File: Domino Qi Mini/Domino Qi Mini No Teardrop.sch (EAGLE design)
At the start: 90 parts, among them J1 MH22-1, J2 MH22-1, M1 DOMINO, Q1 AP2302GN, Q2 2SC4081, SW1 IT-1210, SW2 IT-1210, SW3 IT-1210, U1 MP65151DJ, U2 ATMEGA32U4-XUAU/MU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

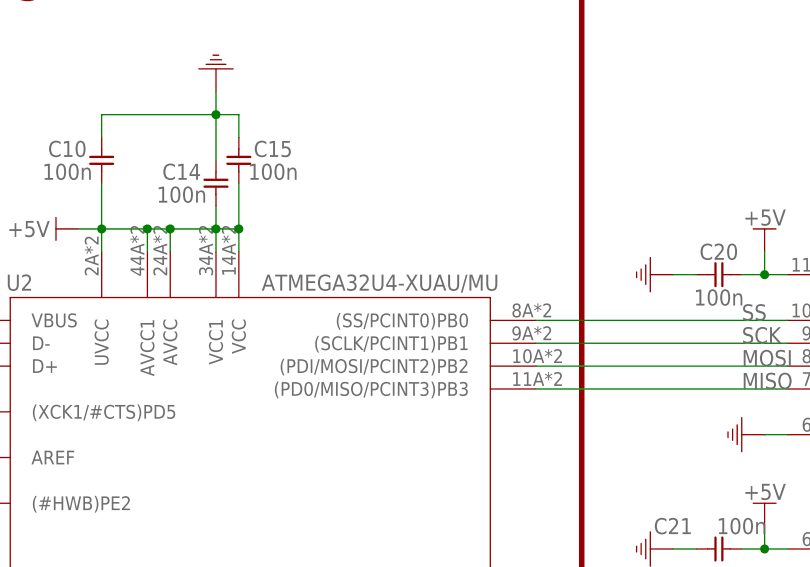
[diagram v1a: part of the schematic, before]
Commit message: Domino Qi Mini Rev. A: added BOM and a few datasheets
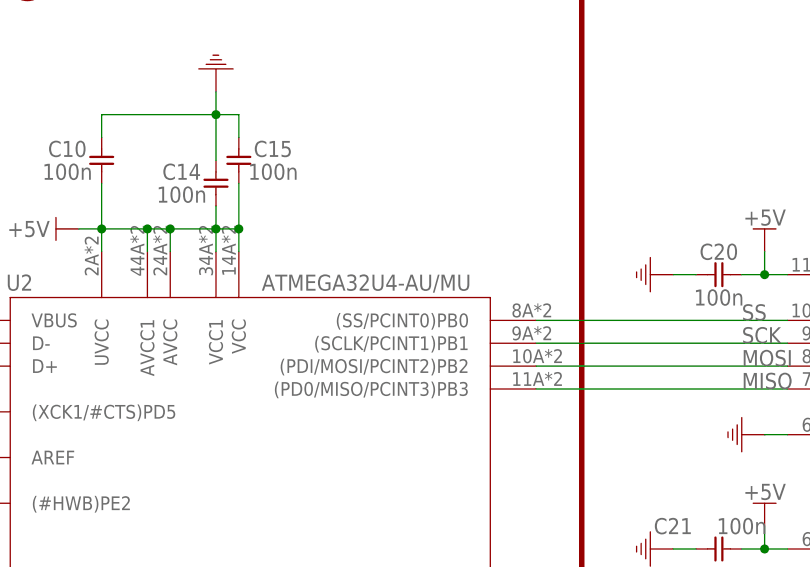
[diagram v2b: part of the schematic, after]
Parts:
- A1: BOM (none) -> EXCLUDE; PARTNO (none) -> RF_ANT1
- C8: PARTNO C0402_2u2_X5R_20%_CER_6V3 -> C0402_2u2_X5R_10%_CER_6V3; TOL ±20% -> ±10%
- J1, J2: PARTNO (none) -> MH22-1-0.1
- Q1: PARTNO (none) -> AP2302GN
- Q2: PARTNO (none) -> 2SC4081
- SW1, SW2, SW3: PARTNO (none) -> IT-1210
- U2: value ATMEGA32U4-XUAU/MU -> ATMEGA32U4-AU/MU; device Domino:ATMEGA32U4-XUAU/MU -> Domino:ATMEGA32U4-AU/MU; PARTNO (none) -> ATMEGA32U4-MU
- U4: PARTNO (none) -> NTB0104GU12
- U5: PARTNO (none) -> NTB0102GU
- U6: PARTNO (none) -> MAX3375EEKA+T
- Y1: PARTNO (none) -> CRYSTAL_16MHZ_32X25_2SH_12PF_30PPM
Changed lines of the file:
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@@
 <?xml version="1.0" encoding="utf-8"?>
 <!DOCTYPE eagle SYSTEM "eagle.dtd">
-<eagle version="7.0.0">
+<eagle version="6.5.0">
 <drawing>
 <settings>
@@
 </part>
 <part name="SUPPLY17" library="Domino" deviceset="GND" device=""/>
-<part name="U2" library="Domino" deviceset="ATMEGA32U4-XU" device="AU/MU" value="ATMEGA32U4-XUAU/MU"/>
+<part name="U2" library="Domino" deviceset="ATMEGA32U4-" device="AU/MU" value="ATMEGA32U4-AU/MU">
+<attribute name="PARTNO" value="ATMEGA32U4-MU"/>
+</part>
 <part name="U$8" library="Domino" deviceset="+5V" device=""/>
 <part name="C15" library="Domino" deviceset="CAP_" device="0402" value="100n">
@@
 <attribute name="VOLT" value="50V"/>
 </part>
-<part name="Y1" library="Domino" deviceset="CRYSTAL_2SH" device="" value="16MHz"/>
+<part name="Y1" library="Domino" deviceset="CRYSTAL_2SH" device="" value="16MHz">
+<attribute name="PARTNO" value="CRYSTAL_16MHZ_32X25_2SH_12PF_30PPM"/>
+</part>
 <part name="R2" library="Domino" deviceset="RES_" device="0402" value="22R">
 <attribute name="PARTNO" value="R0402_22R_5%_62.5mW"/>
@@
 <attribute name="VOLT" value="50V"/>
 </part>
-<part name="U4" library="Domino" deviceset="NTB0104" device="GU12"/>
-<part name="U5" library="Domino" deviceset="NTB0102" device="GU"/>
-<part name="U6" library="Domino" deviceset="MAX3375E" device="EKA+T"/>
+<part name="U4" library="Domino" deviceset="NTB0104" device="GU12">
+<attribute name="PARTNO" value="NTB0104GU12"/>
+</part>
+<part name="U5" library="Domino" deviceset="NTB0102" device="GU">
+<attribute name="PARTNO" value="NTB0102GU"/>
+</part>
+<part name="U6" library="Domino" deviceset="MAX3375E" device="EKA+T">
+<attribute name="PARTNO" value="MAX3375EEKA+T"/>
+</part>
 <part name="U$6" library="Domino" deviceset="+5V" device=""/>
 <part name="U$10" library="Domino" deviceset="+5V" device=""/>
@@
 </part>
 <part name="SUPPLY47" library="Domino" deviceset="GND" device=""/>
-<part name="Q2" library="Domino" deviceset="2SC4081" device=""/>
+<part name="Q2" library="Domino" deviceset="2SC4081" device="">
+<attribute name="PARTNO" value="2SC4081"/>
+</part>
 <part name="R12" library="Domino" deviceset="RES_" device="0402" value="10k">
 <attribute name="PARTNO" value="R0402_10k_5%_62.5mW"/>
@@
 <attribute name="VOLT" value="25V"/>
 </part>
-<part name="Q1" library="Domino" deviceset="AP2302GN" device=""/>
+<part name="Q1" library="Domino" deviceset="AP2302GN" device="">
+<attribute name="PARTNO" value="AP2302GN"/>
+</part>
 <part name="U$16" library="Domino" deviceset="+5V" device=""/>
 <part name="C8" library="Domino" deviceset="CAP_" device="0805" value="2u2">
-<attribute name="PARTNO" value="C0402_2u2_X5R_20%_CER_6V3"/>
+<attribute name="PARTNO" value="C0402_2u2_X5R_10%_CER_6V3"/>
 <attribute name="SIZE" value="0402"/>
 <attribute name="TC" value="X5R"/>
-<attribute name="TOL" value="±20%"/>
+<attribute name="TOL" value="±10%"/>
 <attribute name="TYPE" value="CER"/>
 <attribute name="VOLT" value="6.3V"/>
@@
 <part name="U$2" library="Domino" deviceset="+5V" device=""/>
 <part name="SUPPLY13" library="Domino" deviceset="GND" device=""/>
-<part name="J2" library="Domino" deviceset="MH22-1" device=""/>
-<part name="SW3" library="Domino" deviceset="IT-1210" device=""/>
-<part name="SW2" library="Domino" deviceset="IT-1210" device=""/>
-<part name="SW1" library="Domino" deviceset="IT-1210" device=""/>
+<part name="J2" library="Domino" deviceset="MH22-1" device="">
+<attribute name="PARTNO" value="MH22-1-0.1"/>
+</part>
+<part name="SW3" library="Domino" deviceset="IT-1210" device="">
+<attribute name="PARTNO" value="IT-1210"/>
+</part>
+<part name="SW2" library="Domino" deviceset="IT-1210" device="">
+<attribute name="PARTNO" value="IT-1210"/>
+</part>
+<part name="SW1" library="Domino" deviceset="IT-1210" device="">
+<attribute name="PARTNO" value="IT-1210"/>
+</part>
 <part name="W1" library="Domino" deviceset="DOMINO_QI_LOGO" device=""/>
-<part name="A1" library="Domino" deviceset="RF_ANT1" device=""/>
-<part name="J1" library="Domino" deviceset="MH22-1" device=""/>
+<part name="A1" library="Domino" deviceset="RF_ANT1" device="">
+<attribute name="BOM" value="EXCLUDE"/>
+<attribute name="PARTNO" value="RF_ANT1"/>
+</part>
+<part name="J1" library="Domino" deviceset="MH22-1" device="">
+<attribute name="PARTNO" value="MH22-1-0.1"/>
+</part>
 <part name="C2" library="Domino" deviceset="CAP_" device="0402" value="100n">
 <attribute name="PARTNO" value="C0402_100n_X7R_10%_CER_50V"/>
@@
 <attribute name="VALUE" x="91.44" y="160.02" size="1.778" layer="96" rot="MR180"/>
 <attribute name="NAME" x="66.04" y="158.242" size="1.778" layer="95" rot="MR0"/>
+<attribute name="PARTNO" x="91.44" y="88.9" size="1.778" layer="96" rot="MR0" display="off"/>
 </instance>
 <instance part="U$8" gate="G$1" x="71.12" y="165.1" smashed="yes" rot="R90">
@@
 <attribute name="NAME" x="41.656" y="101.6" size="1.778" layer="95"/>
 <attribute name="VALUE" x="41.656" y="99.06" size="1.778" layer="96"/>
+<attribute name="PARTNO" x="50.8" y="106.68" size="1.778" layer="96" rot="R270" display="off"/>
 </instance>
 <instance part="R2" gate="G$1" x="50.8" y="152.4" smashed="yes">
@@
 <attribute name="NAME" x="154.94" y="165.1" size="1.778" layer="95" rot="MR180" align="center-left"/>
 <attribute name="VALUE" x="162.56" y="165.1" size="1.778" layer="96" rot="MR180" align="center-left"/>
+<attribute name="PARTNO" x="165.1" y="149.86" size="1.778" layer="96" rot="MR0" display="off"/>
 </instance>
 <instance part="U5" gate="G$1" x="165.1" y="121.92" smashed="yes" rot="MR0">
 <attribute name="NAME" x="154.94" y="134.62" size="1.778" layer="95" rot="MR180" align="center-left"/>
 <attribute name="VALUE" x="162.56" y="134.62" size="1.778" layer="96" rot="MR180" align="center-left"/>
+<attribute name="PARTNO" x="165.1" y="121.92" size="1.778" layer="96" rot="MR0" display="off"/>
 </instance>
 <instance part="U6" gate="G$1" x="167.64" y="101.6" smashed="yes">
 <attribute name="NAME" x="154.94" y="111.76" size="1.778" layer="95" align="center-left"/>
 <attribute name="VALUE" x="162.56" y="111.76" size="1.778" layer="96" align="center-left"/>
+<attribute name="PARTNO" x="167.64" y="101.6" size="1.778" layer="96" display="off"/>
 </instance>
 <instance part="U$6" gate="G$1" x="147.32" y="162.56" smashed="yes">
@@
 <attribute name="NAME" x="170.18" y="83.82" size="1.778" layer="95" rot="MR0"/>
 <attribute name="VALUE" x="170.18" y="81.28" size="1.778" layer="96" rot="MR0"/>
+<attribute name="PARTNO" x="172.72" y="83.82" size="1.778" layer="96" rot="MR0" display="off"/>
 </instance>
 <instance part="R12" gate="G$1" x="162.56" y="93.98" smashed="yes" rot="R180">
@@
 <attribute name="VALUE" x="163.83" y="39.37" size="1.778" layer="96" rot="MR0" align="center"/>
 <attribute name="NAME" x="163.83" y="41.91" size="1.778" layer="95" rot="MR0" align="center"/>
+<attribute name="PARTNO" x="157.48" y="35.56" size="1.778" layer="96" rot="MR0" display="off"/>
 </instance>
 <instance part="U$16" gate="G$1" x="55.88" y="175.26" smashed="yes">
@@
 <attribute name="VALUE" x="318.135" y="40.64" size="1.778" layer="96" rot="R180" align="center"/>
 <attribute name="NAME" x="314.96" y="43.053" size="1.778" layer="95" rot="R180" align="center"/>
+<attribute name="PARTNO" x="281.94" y="43.18" size="1.778" layer="96" rot="R90" display="off"/>
 </instance>
 <instance part="SW3" gate="G$1" x="299.72" y="185.42" smashed="yes" rot="MR0">
 <attribute name="NAME" x="302.26" y="193.04" size="1.778" layer="95" rot="MR180"/>
 <attribute name="VALUE" x="302.26" y="190.5" size="1.778" layer="96" rot="MR180"/>
+<attribute name="PARTNO" x="299.72" y="185.42" size="1.778" layer="96" rot="MR0" display="off"/>
 </instance>
 <instance part="SW2" gate="G$1" x="231.14" y="91.44" smashed="yes">
 <attribute name="NAME" x="228.6" y="99.06" size="1.778" layer="95" rot="R180"/>
 <attribute name="VALUE" x="228.6" y="96.52" size="1.778" layer="96" rot="R180"/>
+<attribute name="PARTNO" x="231.14" y="91.44" size="1.778" layer="96" display="off"/>
 </instance>
 <instance part="SW1" gate="G$1" x="109.22" y="25.4" smashed="yes" rot="MR0">
 <attribute name="NAME" x="106.68" y="30.48" size="1.778" layer="95" rot="MR0"/>
 <attribute name="VALUE" x="106.68" y="27.94" size="1.778" layer="96" rot="MR0"/>
+<attribute name="PARTNO" x="109.22" y="25.4" size="1.778" layer="96" rot="MR0" display="off"/>
 </instance>
 <instance part="W1" gate="G$1" x="223.52" y="12.7"/>
@@
 <attribute name="NAME" x="363.22" y="139.7" size="1.778" layer="95" rot="MR180" align="center-left"/>
 <attribute name="VALUE" x="363.22" y="137.16" size="1.778" layer="96" rot="MR180" align="center-left"/>
+<attribute name="BOM" x="350.52" y="137.16" size="1.778" layer="96" rot="MR270" display="off"/>
+<attribute name="PARTNO" x="350.52" y="137.16" size="1.778" layer="96" rot="MR270" display="off"/>
 </instance>
 <instance part="J1" gate="G$1" x="279.4" y="238.76" smashed="yes" rot="MR270">
 <attribute name="VALUE" x="247.015" y="238.76" size="1.778" layer="96" rot="MR0" align="center"/>
 <attribute name="NAME" x="248.92" y="241.427" size="1.778" layer="95" rot="MR0" align="center"/>
+<attribute name="PARTNO" x="279.4" y="238.76" size="1.778" layer="96" rot="MR270" display="off"/>
 </instance>
 <instance part="C2" gate="G$1" x="12.7" y="236.22" smashed="yes" rot="MR270">
